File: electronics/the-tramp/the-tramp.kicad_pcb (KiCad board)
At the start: 2 copper layers, 80 x 35.6 mm, 15 parts, among them P1 CONN_01X02, P2 CONN_01X02, Q1 MPF102, U1 LM386jjg

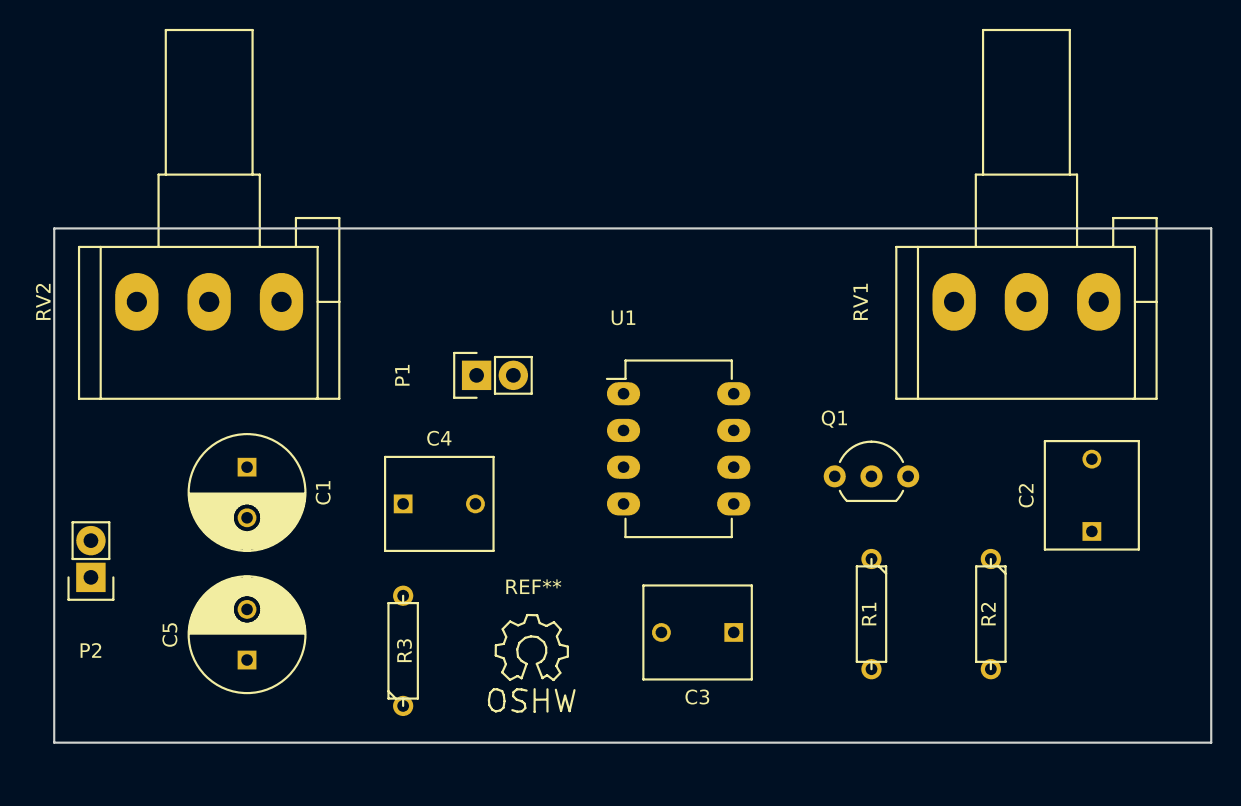
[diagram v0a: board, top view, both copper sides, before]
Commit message: Added power connector and copper fills.
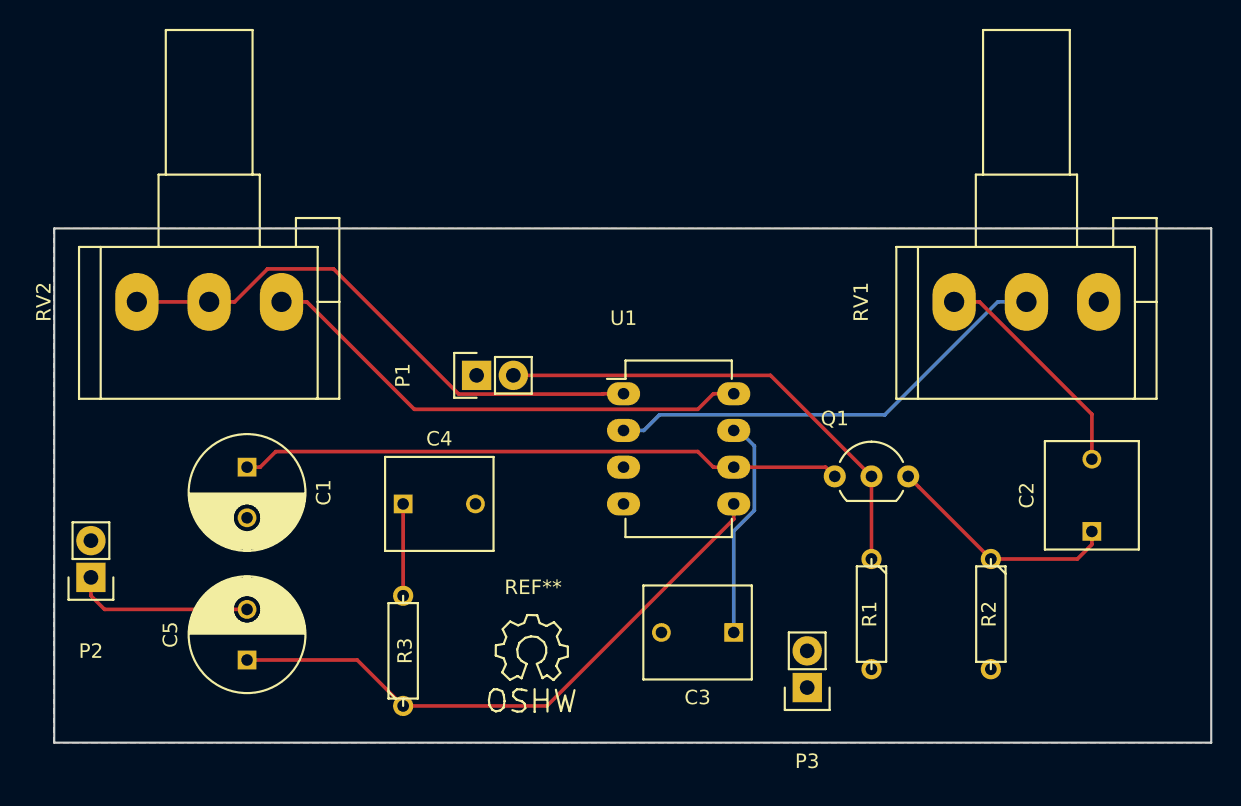
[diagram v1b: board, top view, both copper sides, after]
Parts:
- added P3: CONN_01X02, Pin_Headers:Pin_Header_Straight_1x02, F.Cu at (146.1, 130.8)
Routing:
- net VCC: track 0.00 -> 41.8 mm
- net Net-(C5-Pad1): track 0.00 -> 41.4 mm
- net Net-(RV2-Pad1): track 0.00 -> 38.2 mm
- net Net-(RV2-Pad3): track 0.00 -> 34.8 mm
- net Net-(P1-Pad2): track 0.00 -> 33.4 mm
- net Net-(RV1-Pad2): track 0.00 -> 31.5 mm
- net Net-(C2-Pad1): track 0.00 -> 16.4 mm
- net Net-(C2-Pad2): track 0.00 -> 15.8 mm
- net Net-(C3-Pad1): track 0.00 -> 15.4 mm
- net Net-(C5-Pad2): track 0.00 -> 12.5 mm
- net Net-(C4-Pad1): track 0.00 -> 6.35 mm
- added copper zone on B.Cu, net GND
- added copper zone on F.Cu, net VCC
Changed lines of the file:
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@@
 (kicad_pcb (version 4) (host pcbnew 4.0.2+dfsg1-stable)
   (general
-    (links 25)
-    (no_connects 25)
+    (links 27)
+    (no_connects 0)
     (area 93.904999 98.984999 174.065001 134.695001)
     (thickness 1.6)
     (drawings 4)
-    (tracks 0)
+    (tracks 51)
     (zones 0)
-    (modules 15)
+    (modules 16)
     (nets 13)
   )
@@
     (fp_line (start 0.35052 0.89916) (end 0.7493 1.89992) (layer F.SilkS) (width 0.15))
   )
+  (module Pin_Headers:Pin_Header_Straight_1x02 (layer F.Cu)
+    (at 146.05 130.81 180)
+    (descr "Through hole pin header")
+    (tags "pin header")
+    (fp_text reference P3 (at 0 -5.1 180) (layer F.SilkS)
+      (effects (font (size 1 1) (thickness 0.15)))
+    )
+    (fp_text value CONN_01X02 (at 0 -3.1 180) (layer F.Fab)
+      (effects (font (size 1 1) (thickness 0.15)))
+    )
+    (fp_line (start 1.27 1.27) (end 1.27 3.81) (layer F.SilkS) (width 0.15))
+    (fp_line (start 1.55 -1.55) (end 1.55 0) (layer F.SilkS) (width 0.15))
+    (fp_line (start -1.75 -1.75) (end -1.75 4.3) (layer F.CrtYd) (width 0.05))
+    (fp_line (start 1.75 -1.75) (end 1.75 4.3) (layer F.CrtYd) (width 0.05))
+    (fp_line (start -1.75 -1.75) (end 1.75 -1.75) (layer F.CrtYd) (width 0.05))
+    (fp_line (start -1.75 4.3) (end 1.75 4.3) (layer F.CrtYd) (width 0.05))
+    (fp_line (start 1.27 1.27) (end -1.27 1.27) (layer F.SilkS) (width 0.15))
+    (fp_line (start -1.55 0) (end -1.55 -1.55) (layer F.SilkS) (width 0.15))
+    (fp_line (start -1.55 -1.55) (end 1.55 -1.55) (layer F.SilkS) (width 0.15))
+    (fp_line (start -1.27 1.27) (end -1.27 3.81) (layer F.SilkS) (width 0.15))
+    (fp_line (start -1.27 3.81) (end 1.27 3.81) (layer F.SilkS) (width 0.15))
+    (pad 1 thru_hole rect (at 0 0 180) (size 2.032 2.032) (drill 1.016) (layers *.Cu *.Mask F.SilkS)
+      (net 1 GND))
+    (pad 2 thru_hole oval (at 0 2.54 180) (size 2.032 2.032) (drill 1.016) (layers *.Cu *.Mask F.SilkS)
+      (net 2 VCC))
+    (model Pin_Headers.3dshapes/Pin_Header_Straight_1x02.wrl
+      (at (xyz 0 -0.05 0))
+      (scale (xyz 1 1 1))
+      (rotate (xyz 0 0 90))
+    )
+  )
   (gr_line (start 173.99 99.06) (end 93.98 99.06) (angle 90) (layer Edge.Cuts) (width 0.15))
   (gr_line (start 173.99 134.62) (end 173.99 99.06) (angle 90) (layer Edge.Cuts) (width 0.15))
   (gr_line (start 93.98 134.62) (end 173.99 134.62) (angle 90) (layer Edge.Cuts) (width 0.15))
   (gr_line (start 93.98 99.06) (end 93.98 134.62) (angle 90) (layer Edge.Cuts) (width 0.15))
+  (segment (start 140.97 115.57) (end 147.32 115.57) (width 0.254) (layer F.Cu) (net 2))
+  (segment (start 147.32 115.57) (end 147.955 116.205) (width 0.254) (layer F.Cu) (net 2))
+  (segment (start 107.315 115.57) (end 108.219 115.57) (width 0.254) (layer F.Cu) (net 2))
+  (segment (start 138.48659 114.49059) (end 139.566 115.57) (width 0.254) (layer F.Cu) (net 2))
+  (segment (start 108.219 115.57) (end 109.29841 114.49059) (width 0.254) (layer F.Cu) (net 2))
+  (segment (start 109.29841 114.49059) (end 138.48659 114.49059) (width 0.254) (layer F.Cu) (net 2))
+  (segment (start 139.566 115.57) (end 140.97 115.57) (width 0.254) (layer F.Cu) (net 2))
+  (segment (start 158.75 121.92) (end 164.734 121.92) (width 0.254) (layer F.Cu) (net 3))
+  (segment (start 164.734 121.92) (end 165.735 120.919) (width 0.254) (layer F.Cu) (net 3))
+  (segment (start 165.735 120.919) (end 165.735 120.015) (width 0.254) (layer F.Cu) (net 3))
+  (segment (start 153.035 116.205) (end 153.796999 116.966999) (width 0.254) (layer F.Cu) (net 3))
+  (segment (start 153.796999 116.966999) (end 158.75 121.92) (width 0.254) (layer F.Cu) (net 3))
+  (segment (start 165.735 115.015) (end 165.735 111.91113) (width 0.254) (layer F.Cu) (net 4))
+  (segment (start 165.735 111.91113) (end 157.96387 104.14) (width 0.254) (layer F.Cu) (net 4))
+  (segment (start 157.96387 104.14) (end 156.21 104.14) (width 0.254) (layer F.Cu) (net 4))
+  (segment (start 140.97 127) (end 140.97 119.986516) (width 0.254) (layer B.Cu) (net 5))
+  (segment (start 142.39941 114.10941) (end 141.32 113.03) (width 0.254) (layer B.Cu) (net 5))
+  (segment (start 140.97 119.986516) (end 142.39941 118.557106) (width 0.254) (layer B.Cu) (net 5))
+  (segment (start 142.39941 118.557106) (end 142.39941 114.10941) (width 0.254) (layer B.Cu) (net 5))
+  (segment (start 141.32 113.03) (end 140.97 113.03) (width 0.254) (layer B.Cu) (net 5))
+  (segment (start 118.11 118.11) (end 118.11 124.46) (width 0.254) (layer F.Cu) (net 6))
+  (segment (start 96.52 123.19) (end 96.52 124.46) (width 0.254) (layer F.Cu) (net 7))
+  (segment (start 96.52 124.46) (end 97.465 125.405) (width 0.254) (layer F.Cu) (net 7))
+  (segment (start 97.465 125.405) (end 106.395762 125.405) (width 0.254) (layer F.Cu) (net 7))
+  (segment (start 106.395762 125.405) (end 107.315 125.405) (width 0.254) (layer F.Cu) (net 7))
+  (segment (start 118.11 132.08) (end 128.054 132.08) (width 0.254) (layer F.Cu) (net 8))
+  (segment (start 128.054 132.08) (end 140.97 119.164) (width 0.254) (layer F.Cu) (net 8))
+  (segment (start 140.97 119.164) (end 140.97 118.11) (width 0.254) (layer F.Cu) (net 8))
+  (segment (start 107.315 128.905) (end 114.935 128.905) (width 0.254) (layer F.Cu) (net 8))
+  (segment (start 114.935 128.905) (end 118.11 132.08) (width 0.254) (layer F.Cu) (net 8))
+  (segment (start 150.495 116.205) (end 143.51 109.22) (width 0.254) (layer F.Cu) (net 9))
+  (segment (start 143.51 109.22) (end 125.73 109.22) (width 0.254) (layer F.Cu) (net 9))
+  (segment (start 150.495 121.92) (end 150.495 116.205) (width 0.254) (layer F.Cu) (net 9))
+  (segment (start 161.21126 104.14) (end 159.226661 104.14) (width 0.254) (layer B.Cu) (net 10))
+  (segment (start 134.754 113.03) (end 133.35 113.03) (width 0.254) (layer B.Cu) (net 10))
+  (segment (start 159.226661 104.14) (end 151.416071 111.95059) (width 0.254) (layer B.Cu) (net 10))
+  (segment (start 151.416071 111.95059) (end 135.83341 111.95059) (width 0.254) (layer B.Cu) (net 10))
+  (segment (start 135.83341 111.95059) (end 134.754 113.03) (width 0.254) (layer B.Cu) (net 10))
+  (segment (start 99.695 104.14) (end 104.69626 104.14) (width 0.254) (layer F.Cu) (net 11))
+  (segment (start 104.69626 104.14) (end 106.45013 104.14) (width 0.254) (layer F.Cu) (net 11))
+  (segment (start 106.45013 104.14) (end 108.72979 101.86034) (width 0.254) (layer F.Cu) (net 11))
+  (segment (start 108.72979 101.86034) (end 113.295418 101.86034) (width 0.254) (layer F.Cu) (net 11))
+  (segment (start 113.295418 101.86034) (end 121.950479 110.515401) (width 0.254) (layer F.Cu) (net 11))
+  (segment (start 121.950479 110.515401) (end 131.920599 110.515401) (width 0.254) (layer F.Cu) (net 11))
+  (segment (start 131.920599 110.515401) (end 131.946 110.49) (width 0.254) (layer F.Cu) (net 11))
+  (segment (start 131.946 110.49) (end 133.35 110.49) (width 0.254) (layer F.Cu) (net 11))
+  (segment (start 109.69752 104.14) (end 111.45139 104.14) (width 0.254) (layer F.Cu) (net 12))
+  (segment (start 138.48659 111.56941) (end 139.566 110.49) (width 0.254) (layer F.Cu) (net 12))
+  (segment (start 111.45139 104.14) (end 118.8808 111.56941) (width 0.254) (layer F.Cu) (net 12))
+  (segment (start 118.8808 111.56941) (end 138.48659 111.56941) (width 0.254) (layer F.Cu) (net 12))
+  (segment (start 139.566 110.49) (end 140.97 110.49) (width 0.254) (layer F.Cu) (net 12))
+  (zone (net 1) (net_name GND) (layer B.Cu) (hatch edge 0.508)
+    (connect_pads (clearance 0.508))
+    (min_thickness 0.254)
+    (fill yes (arc_segments 16) (thermal_gap 0.508) (thermal_bridge_width 0.508))
+    (polygon
+      (pts
+        (xy 173.99 134.62) (xy 93.98 134.62) (xy 93.98 99.06) (xy 173.99 99.06) (xy 173.99 134.62)
+      )
+    )
+  )
+  (zone (net 2) (net_name VCC) (layer F.Cu) (hatch edge 0.508)
+    (connect_pads (clearance 0.508))
+    (min_thickness 0.254)
+    (fill yes (arc_segments 16) (thermal_gap 0.508) (thermal_bridge_width 0.508))
+    (polygon
+      (pts
+        (xy 173.99 134.62) (xy 93.98 134.62) (xy 93.98 99.06) (xy 173.99 99.06) (xy 173.99 134.62)
+      )
+    )
+  )
 )
